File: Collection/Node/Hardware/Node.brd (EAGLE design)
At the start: 160 x 100 mm, 13 parts, among them IC1 4050D, IC2 LP298XS, IC3 DS3231/SO, M2 WIRELESS-NRF24L01-PA-EXT, U2 ATMEGA328P-PU, X1 MICROSD

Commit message: Updated schematic
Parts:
- added C1, C2, C3, C4: 22pF, rcl:C050-035X075
- added Q1: 16MHz, crystal:HC49/S
- added R2: 10K, rcl:R0805
- added SW2: FSMSM, Switch:FSMSM
- R3, R4: value (none) -> 10K
- moved J3 114.1 mm to (2.54, 24.1), turned to 270 degrees
- moved R1 90.8 mm to (11.4, 22.9)
- moved R3 84.6 mm to (11.4, 25.4)
- moved B1 83.9 mm to (7.62, 64.8), turned to 90 degrees
- moved R4 79.4 mm to (11.4, 27.9)
- moved X1 68.1 mm to (1.27, 17.8)
- moved IC1 62.0 mm to (20.3, 29.2), turned to 270 degrees
- moved J2 61.5 mm to (2.54, 34.3), turned to 270 degrees
- moved IC2 60.2 mm to (35.6, 57.1)
- moved M2 53.0 mm to (35.6, 21.6), turned to 270 degrees
- moved IC3 51.5 mm to (24.1, 63.5), turned to 180 degrees
- moved ACT 49.5 mm to (35.6, 66.0)
- moved U2 22.9 mm to (21.6, 48.3), turned to 270 degrees
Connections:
- removed net AVCC: U2.20
- new net N$6: R2.1, SW2.1, U2.1
- new net N$7: C1.1, Q1.1, U2.10
- new net N$8: C2.1, Q1.2, U2.9
- net +3V3: now also C4.1
- net +5V: now also C3.1, R2.2, U2.20
- net GND: now also C1.2, C2.2, C3.2, C4.2, SW2.2, U2.21
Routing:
- net N$6: track 0.00 -> 74.2 mm, vias 0 -> 2
- net N$4: track 5.78 -> 68.0 mm
- net N$3: track 84.1 -> 27.8 mm
- net N$8: track 0.00 -> 42.1 mm
- net N$7: track 0.00 -> 35.3 mm, vias 0 -> 1
- net N$5: track 60.3 -> 26.9 mm, vias 0 -> 2
- net SDA: track 105.9 -> 74.5 mm
- net GND: track 173.6 -> 202.9 mm, vias 1 -> 0
- net N$2: track 60.4 -> 32.1 mm
- net +3V3: track 116.7 -> 88.5 mm, vias 0 -> 2
- net N$1: track 38.7 -> 52.7 mm
- net CE: track 52.0 -> 38.2 mm
- net SCK: track 33.1 -> 20.9 mm
- net MISO: track 33.1 -> 20.9 mm
- net MOSI: track 39.3 -> 27.0 mm
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
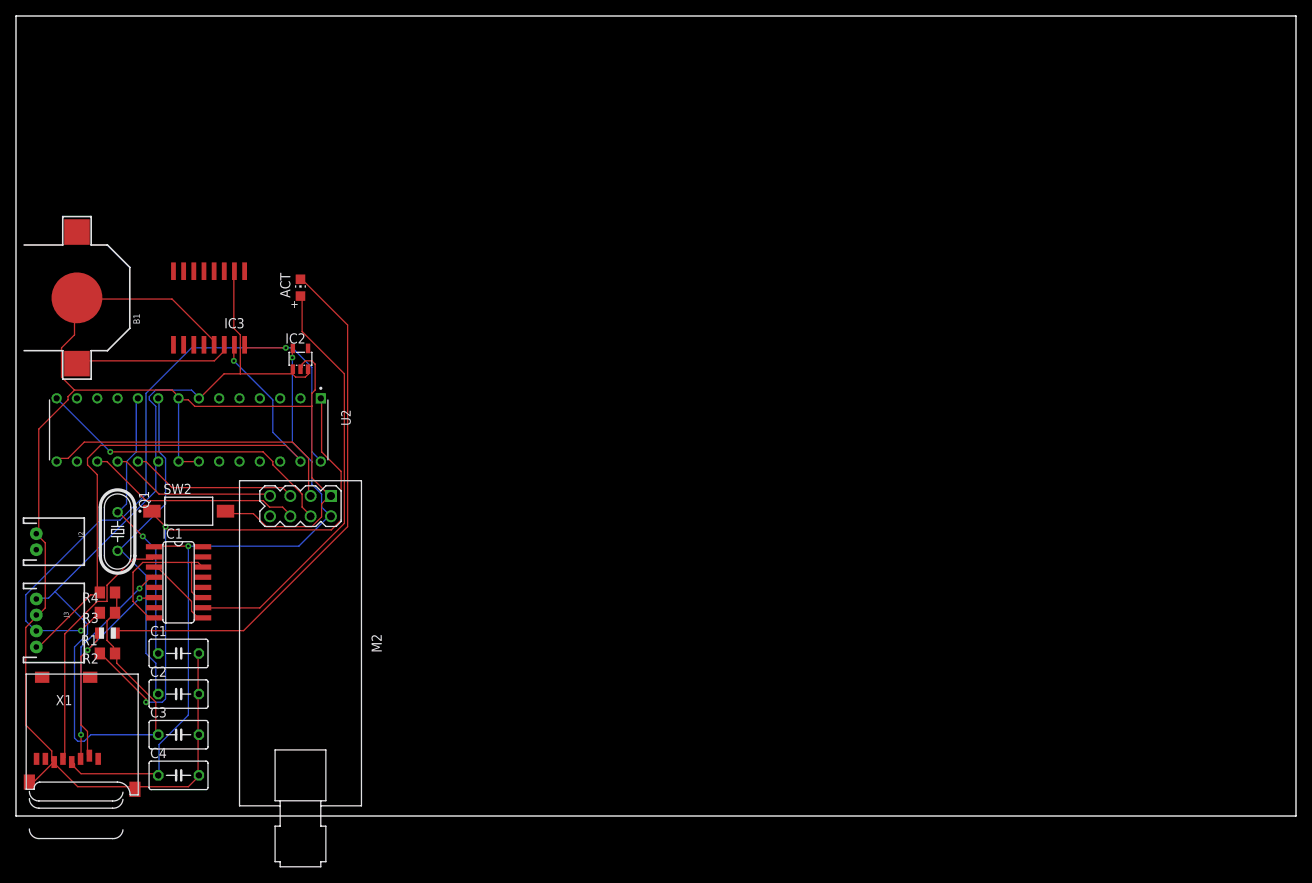
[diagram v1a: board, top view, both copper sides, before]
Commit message: Adjusted board size
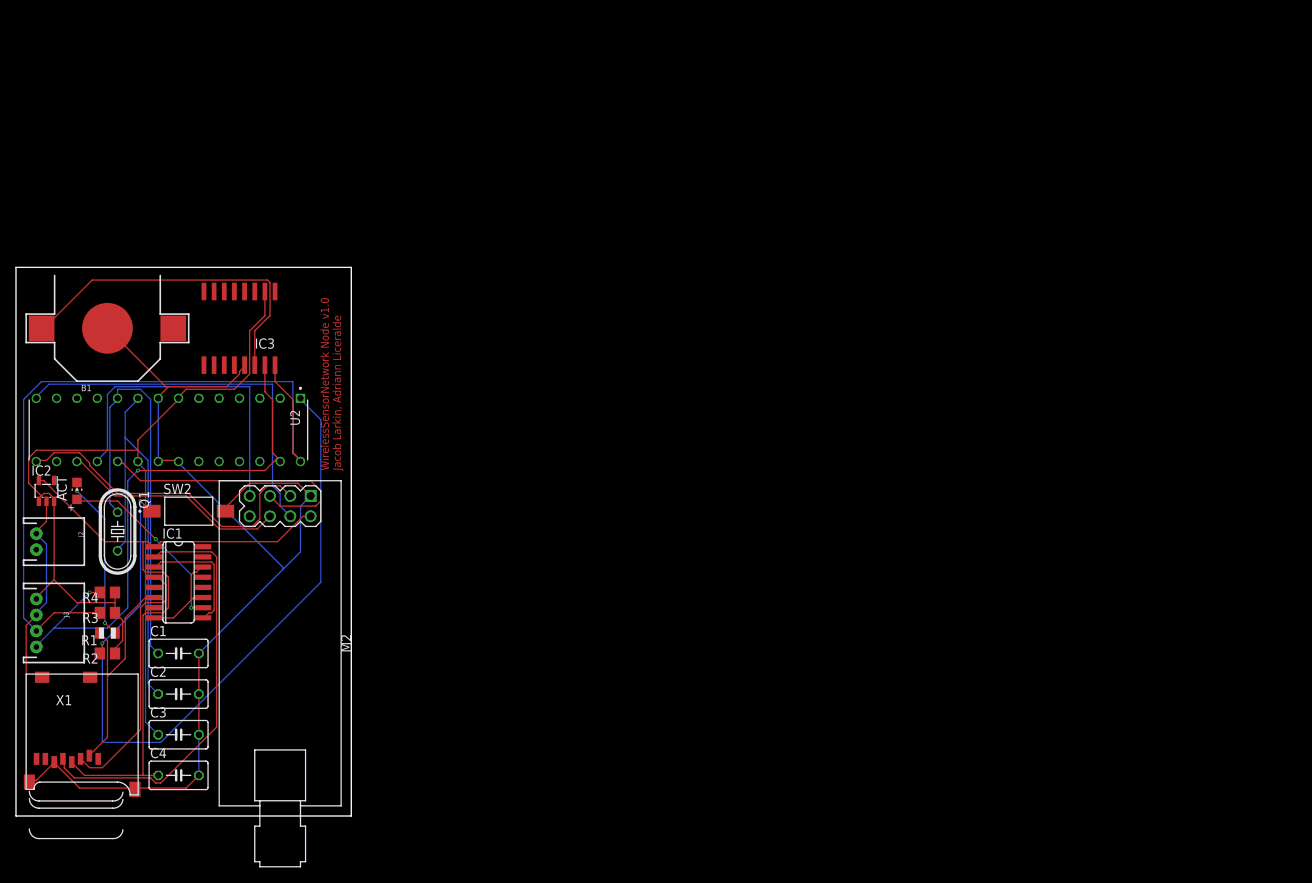
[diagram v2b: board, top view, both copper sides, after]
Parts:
- C3, C4: value 22pF -> .1uF
- moved ACT 37.8 mm to (7.62, 40.6)
- moved IC2 35.8 mm to (3.81, 40.6)
- moved B1 5.39 mm to (11.4, 61.0), turned to 0 degrees
- moved IC3 4.58 mm to (27.9, 61.0)
- moved M2 2.54 mm to (33.0, 21.6)
- moved U2 2.54 mm to (19.1, 48.3)
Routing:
- net N$4: track 68.0 -> 20.9 mm, vias 0 -> 2
- net GND: track 202.9 -> 168.9 mm
- net N$1: track 52.7 -> 23.9 mm, vias 0 -> 2
- net VBAT: track 19.9 -> 42.3 mm
- net N$2: track 32.1 -> 53.5 mm
- net N$6: track 74.2 -> 95.3 mm
- net MISO: track 20.9 -> 40.7 mm
- net N$7: track 35.3 -> 53.0 mm, vias 1 -> 0
- net SCK: track 20.9 -> 35.4 mm
- net N$8: track 42.1 -> 53.9 mm
- net GND_SD: track 22.1 -> 12.3 mm
- net CSN: track 39.1 -> 47.8 mm, vias 1 -> 0
- net SCL: track 88.4 -> 96.8 mm, vias 2 -> 0
- net CLK: track 9.48 -> 15.4 mm
- net N$5: track 26.9 -> 32.5 mm, vias 2 -> 0
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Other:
- board size 160 x 100 mm -> 41.9 x 68.6 mm
- board text added: "WirelessSensorNetwork Node v1.0 Jacob Larkin, Adriann Liceralde"

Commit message: updated schematic
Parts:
- removed ACT: RED, adafruit:CHIP-LED0805
- removed B1: CR1220, microbuilder:CR1220
- removed J2: (no value), SparkFun-Connectors:JST-2-PTH
- removed J3: (no value), SparkFun-Connectors:JST-4-PTH
- removed X1: MICROSD, adafruit:MICROSD
- added BT1: KEYSTONE_ELECTRONICS_3034KEYSTONE_ELECTRONICS_3034_0_0, Keystone Electronics - 3034:KEYSTONE_ELECTRONICS_3034_0
- added H1, H2: MOUNT-PAD-ROUND3.0, holes:3,0-PAD
- added JP1, JP3: (no value), pinhead:1X02
- added JP2: (no value), pinhead:1X04
- added LED1: RED, led:CHIPLED_0805
- added LED2: GREEN, led:CHIPLED_0805
- added LED3: Yellow, led:CHIPLED_0805
- added R5, R6: 1K, rcl:R0805
- added U$1: 1051620001A, Molex_micro_SD:1051620001_SMT
- C1, C2, C3, C4: device rcl:C050-035X075 -> rcl:C0805
- Q1: device crystal:HC49/S -> special:QS
- R1: device adafruit:R0805 -> rcl:R0805
- moved IC3 32.6 mm to (6.73, 36.2), turned to 0 degrees
- moved R3 32.3 mm to (2.41, 56.4), turned to 90 degrees
- moved R4 29.2 mm to (4.95, 56.4), turned to 90 degrees
- moved C2 20.0 mm to (15.1, 34.5), turned to 270 degrees
- moved IC2 19.1 mm to (14.6, 24.9), turned to 90 degrees
- moved IC1 16.2 mm to (6.35, 21.1), turned to 0 degrees
- moved C4 15.6 mm to (20.7, 20.7), turned to 270 degrees
- moved C1 14.4 mm to (17.9, 34.5), turned to 270 degrees
- moved C3 11.0 mm to (23.5, 20.7), turned to 270 degrees
- moved SW2 9.04 mm to (18.5, 29.6)
- moved Q1 7.29 mm to (18.7, 39.8), turned to 180 degrees
- moved R1 6.83 mm to (17.9, 20.7), turned to 90 degrees
- moved R2 3.70 mm to (15.1, 20.7), turned to 270 degrees
- moved U2 0.40 mm to (18.9, 47.9), turned to 90 degrees
- moved M2 0.13 mm to (33.0, 21.7)
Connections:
- removed net CD: X1.CD1
- removed net GND_SD: IC1.11, IC1.14, IC1.8
- removed net V_EXTERNAL_BATTERY: J2.2
- new net N$10: LED2.A, R5.1
- new net N$11: LED3.A, R6.1
- new net N$12: R6.2, U2.12
- new net N$9: R5.2, U2.11
- new net V_PACK: JP1.1
- net +3V3: now also U$1.4; no longer X1.4
- net +5V: now also JP2.4; no longer J3.1
- net DO: now also U$1.7; no longer X1.7
- net GND: now also BT1.1, IC1.11, IC1.14, IC1.8, JP1.2, JP2.3, JP3.2, LED2.C, LED3.C, U$1.6, U$1.G1, U$1.G2, U$1.G3, U$1.G4; no longer B1.-, J2.1, J3.2, X1.6, X1.MT1, X1.MT2
- net N$1: now also LED1.A; no longer ACT.A
- net N$2: now also U$1.5; no longer X1.5
- net N$3: now also U$1.2; no longer X1.2
- net N$4: now also LED1.C; no longer ACT.C
- net N$5: now also U$1.3; no longer X1.3
- net SCL: now also JP2.2; no longer J3.3
- net SDA: now also JP2.1; no longer J3.4
- net VBAT: now also BT1.2, BT1.2-2; no longer B1.+$1
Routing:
- net SCL: track 96.8 -> 30.7 mm
- net N$6: track 95.3 -> 29.4 mm
- net N$7: track 53.0 -> 11.6 mm
- net CSN: track 47.8 -> 6.86 mm
- net N$8: track 53.9 -> 13.0 mm
- net N$2: track 53.5 -> 13.3 mm, vias 0 -> 2
- net SDA: track 70.3 -> 31.1 mm, vias 2 -> 0
- net CE: track 40.8 -> 12.2 mm
- net MISO: track 40.7 -> 14.0 mm
- net GND: track 168.9 -> 142.8 mm, vias 0 -> 3
- net SCK: track 35.4 -> 17.4 mm
- net N$4: track 20.9 -> 3.15 mm, vias 2 -> 0
- net VBAT: track 42.3 -> 58.6 mm
- net N$5: track 32.5 -> 17.3 mm, vias 0 -> 2
- net N$1: track 23.9 -> 11.6 mm
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- added copper zone on layer 16, net GND
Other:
- board size 41.9 x 68.6 mm -> 41.9 x 77.5 mm
- board text added: "External Battery"
- board text added: "Node v1.0 WirelessSensorNetwork Jacob Larkin, Adriann Liceralde"
- board text added: "Solar Panel"
- board text removed: "WirelessSensorNetwork Node v1.0 Jacob Larkin, Adriann Liceralde"
